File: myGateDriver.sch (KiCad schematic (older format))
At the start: 86 parts, among them Q5 BC817, Q8 TIP41, Q9 TIP42, U2 6N136S, U3 PC817

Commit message: fuse added
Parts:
- removed C?: 100nF, Capacitor_SMD:C_1206_3216Metric_Pad1.33x1.80mm_HandSolder, symbol Device:C
- removed C?: 10uf/35v, Capacitor_THT:CP_Radial_D8.0mm_P3.80mm, symbol Device:CP
- removed CmirrorCurrentProtection: 22nF, Capacitor_SMD:C_1206_3216Metric_Pad1.33x1.80mm_HandSolder, symbol Device:C
- removed D?: 1.5KE10A, Diode_THT:D_DO-201AD_P5.08mm_Vertical_AnodeUp, symbol Diode:1.5KExxA
- removed D?: BYV26E, Diode_THT:D_DO-201AD_P5.08mm_Vertical_AnodeUp, symbol Simulation_SPICE:DIODE
- removed D?: Dz17v, Diode_THT:D_DO-201AD_P5.08mm_Vertical_AnodeUp, symbol Diode:1.5KExxA
- removed Dex3, Dex4: 1n4148, Diode_SMD:D_SMA, symbol Device:D_Schottky
- removed Q? (x3), QDynamicVCE: BC807, Package_TO_SOT_SMD:SOT-23, symbol Transistor_BJT:BC807
- removed Q?: BC817, Package_TO_SOT_SMD:SOT-23, symbol Transistor_BJT:BC817
- removed R10: 220, Resistor_THT:R_Axial_DIN0207_L6.3mm_D2.5mm_P10.16mm_Horizontal, symbol Device:R
- removed Rex?: 1k, Resistor_THT:R_Axial_DIN0207_L6.3mm_D2.5mm_P10.16mm_Horizontal, symbol Device:R
- removed Rex?: 6.8k, Resistor_THT:R_Axial_DIN0207_L6.3mm_D2.5mm_P10.16mm_Horizontal, symbol Device:R
- added D?: 1.5KE6V8A, Diode_THT:D_DO-201AD_P5.08mm_Vertical_AnodeUp, symbol Diode:1.5KExxA
- added F?: Fuse, symbol Device:Fuse
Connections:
- net GND-p: now also Q9.2 (C); no longer Q9.3 (E)
- net Gate: now also JP1.1 (A)
- net Vpp: now also Q5.3 (C), F?.1
- net at CDynamic1.2, DzDynamic1.2 (A2), RDynamic1.2: now also R7.1; no longer JP1.2 (C)
- net Control: now reaches JP1.3 (B)
- net Control: now also CsoftTurnOff2.2, Q8.1 (B), Q9.1 (B), RsoftTurnoff2.2; no longer R7.1
- net at R7.2: now also D?.2 (A2)
- net at Roff1.2: now also Q9.3 (E); no longer Q9.2 (C)
- new net: D?.1 (A1), JP1.2 (C)
- new net Vin: F?.2
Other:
- note added: "Active VCE protection"
- note added: "Control Circuit"
- note added: "Power stage"
- note added: "Under voltage protection"
- note added: "input voltage protection"
- note added: "trun off gate clamp"
- moved on the sheet: C1, C2, C5, C?, CDynamic1, CShortPulseFilter1, CblankTime1, Cclamp1, Cex1, Cex2, CsoftTurnOff2, CsoftTurnOffTiming1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

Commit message: skm200 3d
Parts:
- added SYM1: SYM_Arrow45_Normal, IGBT-DRIVER-emad:skm200GB, symbol Graphic:SYM_Arrow45_Normal
- gave numbers to parts that had none: 11
- renumbered DZunderVoltageFault to DZunderVoltageFault1, DprotectionHigh to DprotectionHigh1, DprotectionLow to DprotectionLow1, QfaultLatch to QfaultLatch1, QsoftTurnOnn to QsoftTurnOnn1
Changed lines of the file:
@@
 P 14450 4875
 AR Path="/630D95A8" Ref="D?"  Part="1"
-AR Path="/6309618D/630D95A8" Ref="DZunderVoltageFault"  Part="1"
+AR Path="/6309618D/630D95A8" Ref="DZunderVoltageFault1"  Part="1"
 AR Path="/63385DDA/630D95A8" Ref="D?"  Part="1"
 AR Path="/6340E1F3/630D95A8" Ref="D22"  Part="1"
-F 0 "DZunderVoltageFault" H 13955 4770 50  0000 L CNN
+F 0 "DZunderVoltageFault1" H 13955 4770 50  0000 L CNN
 F 1 "BZX85C20" H 14250 4985 50  0000 L CNN
 F 2 "Diode_SMD:D_MELF" H 14450 4700 50  0001 C CNN
@@
 P 5865 7905
 AR Path="/630D96CE" Ref="Q?"  Part="1"
-AR Path="/6309618D/630D96CE" Ref="QfaultLatch"  Part="1"
+AR Path="/6309618D/630D96CE" Ref="QfaultLatch1"  Part="1"
 AR Path="/63385DDA/630D96CE" Ref="Q?"  Part="1"
 AR Path="/6340E1F3/630D96CE" Ref="Q17"  Part="1"
-F 0 "QfaultLatch" H 5500 8095 50  0000 L CNN
+F 0 "QfaultLatch1" H 5500 8095 50  0000 L CNN
 F 1 "BC807" H 5610 7760 50  0000 L CNN
 F 2 "Package_TO_SOT_SMD:SOT-23" H 6065 7830 50  0001 L CIN
@@
 P 12755 7520
 AR Path="/61915D54" Ref="Dex?"  Part="1"
-AR Path="/6309618D/61915D54" Ref="DprotectionHigh"  Part="1"
+AR Path="/6309618D/61915D54" Ref="DprotectionHigh1"  Part="1"
 AR Path="/63385DDA/61915D54" Ref="Dex?"  Part="1"
-AR Path="/6340E1F3/61915D54" Ref="Dex?"  Part="1"
-F 0 "DprotectionHigh" H 12675 7625 50  0000 C CNN
+AR Path="/6340E1F3/61915D54" Ref="Dex3"  Part="1"
+F 0 "DprotectionHigh1" H 12675 7625 50  0000 C CNN
 F 1 "1n4148" H 12755 7410 50  0000 C CNN
 F 2 "Diode_SMD:D_SMA" H 12755 7520 50  0001 C CNN
@@
 P 12755 8460
 AR Path="/61941051" Ref="Dex?"  Part="1"
-AR Path="/6309618D/61941051" Ref="DprotectionLow"  Part="1"
+AR Path="/6309618D/61941051" Ref="DprotectionLow1"  Part="1"
 AR Path="/63385DDA/61941051" Ref="Dex?"  Part="1"
-AR Path="/6340E1F3/61941051" Ref="Dex?"  Part="1"
-F 0 "DprotectionLow" H 12745 8565 50  0000 C CNN
+AR Path="/6340E1F3/61941051" Ref="Dex4"  Part="1"
+F 0 "DprotectionLow1" H 12745 8565 50  0000 C CNN
 F 1 "1n4148" H 12755 8350 50  0000 C CNN
 F 2 "Diode_SMD:D_SMA" H 12755 8460 50  0001 C CNN
@@
 P 8005 4040
 AR Path="/61958594" Ref="D?"  Part="1"
-AR Path="/6309618D/61958594" Ref="D?"  Part="1"
+AR Path="/6309618D/61958594" Ref="D7"  Part="1"
 AR Path="/63385DDA/61958594" Ref="D?"  Part="1"
-AR Path="/6340E1F3/61958594" Ref="D?"  Part="1"
-F 0 "D?" V 7920 3995 50  0000 L CNN
+AR Path="/6340E1F3/61958594" Ref="D15"  Part="1"
+F 0 "D7" V 7920 3995 50  0000 L CNN
 F 1 "26v TVS" V 8100 3885 50  0000 L CNN
 F 2 "Diode_SMD:D_MELF" H 8005 3865 50  0001 C CNN
@@
 P 8500 4050
 AR Path="/619A6A28" Ref="C?"  Part="1"
-AR Path="/6309618D/619A6A28" Ref="C?"  Part="1"
+AR Path="/6309618D/619A6A28" Ref="C22"  Part="1"
 AR Path="/63385DDA/619A6A28" Ref="C?"  Part="1"
-AR Path="/6340E1F3/619A6A28" Ref="C?"  Part="1"
-F 0 "C?" H 8505 3985 50  0000 C CNN
+AR Path="/6340E1F3/619A6A28" Ref="C24"  Part="1"
+F 0 "C22" H 8505 3985 50  0000 C CNN
 F 1 "100nF" H 8480 4135 50  0000 C CNN
 F 2 "Capacitor_SMD:C_1206_3216Metric_Pad1.33x1.80mm_HandSolder" H 8538 3900 50  0001 C CNN
@@
 P 7530 4050
 AR Path="/619A742B" Ref="C?"  Part="1"
-AR Path="/6309618D/619A742B" Ref="C?"  Part="1"
+AR Path="/6309618D/619A742B" Ref="C21"  Part="1"
 AR Path="/63385DDA/619A742B" Ref="C?"  Part="1"
-AR Path="/6340E1F3/619A742B" Ref="C?"  Part="1"
-F 0 "C?" H 7525 4125 50  0000 C CNN
+AR Path="/6340E1F3/619A742B" Ref="C23"  Part="1"
+F 0 "C21" H 7525 4125 50  0000 C CNN
 F 1 "47uf/35v" H 7520 3965 50  0000 C CNN
 F 2 "Capacitor_THT:CP_Radial_D8.0mm_P3.80mm" H 7568 3900 50  0001 C CNN
@@
 P 6525 7050
 AR Path="/619F7C8A" Ref="Q?"  Part="1"
-AR Path="/6309618D/619F7C8A" Ref="Q?"  Part="1"
+AR Path="/6309618D/619F7C8A" Ref="Q2"  Part="1"
 AR Path="/63385DDA/619F7C8A" Ref="Q?"  Part="1"
-AR Path="/6340E1F3/619F7C8A" Ref="Q?"  Part="1"
-F 0 "Q?" H 6716 7096 50  0000 L CNN
+AR Path="/6340E1F3/619F7C8A" Ref="Q12"  Part="1"
+F 0 "Q2" H 6716 7096 50  0000 L CNN
 F 1 "BC817" H 6716 7005 50  0000 L CNN
 F 2 "Package_TO_SOT_SMD:SOT-23" H 6725 6975 50  0001 L CIN
@@
 P 6160 8840
 AR Path="/619FC086" Ref="Q?"  Part="1"
-AR Path="/6309618D/619FC086" Ref="QsoftTurnOnn"  Part="1"
+AR Path="/6309618D/619FC086" Ref="QsoftTurnOnn1"  Part="1"
 AR Path="/63385DDA/619FC086" Ref="Q?"  Part="1"
-AR Path="/6340E1F3/619FC086" Ref="Q?"  Part="1"
-F 0 "QsoftTurnOnn" H 6351 8886 50  0000 L CNN
+AR Path="/6340E1F3/619FC086" Ref="Q11"  Part="1"
+F 0 "QsoftTurnOnn1" H 6351 8886 50  0000 L CNN
 F 1 "BC817" H 6351 8795 50  0000 L CNN
 F 2 "Package_TO_SOT_SMD:SOT-23" H 6360 8765 50  0001 L CIN
@@
 P 4655 8770
 AR Path="/619FCED8" Ref="Q?"  Part="1"
-AR Path="/6309618D/619FCED8" Ref="Q?"  Part="1"
+AR Path="/6309618D/619FCED8" Ref="Q1"  Part="1"
 AR Path="/63385DDA/619FCED8" Ref="Q?"  Part="1"
-AR Path="/6340E1F3/619FCED8" Ref="Q?"  Part="1"
-F 0 "Q?" H 4846 8816 50  0000 L CNN
+AR Path="/6340E1F3/619FCED8" Ref="Q10"  Part="1"
+F 0 "Q1" H 4846 8816 50  0000 L CNN
 F 1 "BC817" H 4846 8725 50  0000 L CNN
 F 2 "Package_TO_SOT_SMD:SOT-23" H 4855 8695 50  0001 L CIN
@@
 P 14085 5120
 AR Path="/619FDDB9" Ref="Q?"  Part="1"
-AR Path="/6309618D/619FDDB9" Ref="Q?"  Part="1"
+AR Path="/6309618D/619FDDB9" Ref="Q7"  Part="1"
 AR Path="/63385DDA/619FDDB9" Ref="Q?"  Part="1"
-AR Path="/6340E1F3/619FDDB9" Ref="Q?"  Part="1"
-F 0 "Q?" H 14276 5166 50  0000 L CNN
+AR Path="/6340E1F3/619FDDB9" Ref="Q18"  Part="1"
+F 0 "Q7" H 14276 5166 50  0000 L CNN
 F 1 "BC817" H 14276 5075 50  0000 L CNN
 F 2 "Package_TO_SOT_SMD:SOT-23" H 14285 5045 50  0001 L CIN
@@
 P 11195 4560
 AR Path="/619FFBE7" Ref="Q?"  Part="1"
-AR Path="/6309618D/619FFBE7" Ref="Q?"  Part="1"
+AR Path="/6309618D/619FFBE7" Ref="Q6"  Part="1"
 AR Path="/63385DDA/619FFBE7" Ref="Q?"  Part="1"
-AR Path="/6340E1F3/619FFBE7" Ref="Q?"  Part="1"
-F 0 "Q?" H 11386 4606 50  0000 L CNN
+AR Path="/6340E1F3/619FFBE7" Ref="Q15"  Part="1"
+F 0 "Q6" H 11386 4606 50  0000 L CNN
 F 1 "BC817" H 11386 4515 50  0000 L CNN
 F 2 "Package_TO_SOT_SMD:SOT-23" H 11395 4485 50  0001 L CIN
@@
 P 10780 5000
 AR Path="/61A017AB" Ref="Q?"  Part="1"
-AR Path="/6309618D/61A017AB" Ref="Q?"  Part="1"
+AR Path="/6309618D/61A017AB" Ref="Q3"  Part="1"
 AR Path="/63385DDA/61A017AB" Ref="Q?"  Part="1"
-AR Path="/6340E1F3/61A017AB" Ref="Q?"  Part="1"
-F 0 "Q?" H 10971 5046 50  0000 L CNN
+AR Path="/6340E1F3/61A017AB" Ref="Q13"  Part="1"
+F 0 "Q3" H 10971 5046 50  0000 L CNN
 F 1 "BC817" H 10971 4955 50  0000 L CNN
 F 2 "Package_TO_SOT_SMD:SOT-23" H 10980 4925 50  0001 L CIN
@@
 P 11170 8135
 AR Path="/61926996" Ref="Q?"  Part="1"
-AR Path="/6309618D/61926996" Ref="Q?"  Part="1"
+AR Path="/6309618D/61926996" Ref="Q4"  Part="1"
 AR Path="/63385DDA/61926996" Ref="Q?"  Part="1"
-AR Path="/6340E1F3/61926996" Ref="Q?"  Part="1"
-F 0 "Q?" H 11050 8255 50  0000 L CNN
+AR Path="/6340E1F3/61926996" Ref="Q14"  Part="1"
+F 0 "Q4" H 11050 8255 50  0000 L CNN
 F 1 "BC807" H 11000 7985 50  0000 L CNN
 F 2 "Package_TO_SOT_SMD:SOT-23" H 11370 8060 50  0001 L CIN
@@
 P 4675 1585
 AR Path="/61A66FE0" Ref="D?"  Part="1"
-AR Path="/6309618D/61A66FE0" Ref="D?"  Part="1"
+AR Path="/6309618D/61A66FE0" Ref="D6"  Part="1"
 AR Path="/63385DDA/61A66FE0" Ref="D?"  Part="1"
-AR Path="/6340E1F3/61A66FE0" Ref="D?"  Part="1"
-F 0 "D?" H 4675 1802 50  0000 C CNN
+AR Path="/6340E1F3/61A66FE0" Ref="D12"  Part="1"
+F 0 "D6" H 4675 1802 50  0000 C CNN
 F 1 "1.5KE6V8A" H 4675 1711 50  0000 C CNN
 F 2 "Diode_THT:D_DO-201AD_P5.08mm_Vertical_AnodeUp" H 4675 1385 50  0001 C CNN
@@
 Vin
 $Comp
-L Device:Fuse F?
+L Device:Fuse F2
 U 1 1 61AD0B07
 P 7665 3540
-F 0 "F?" V 7468 3540 50  0000 C CNN
+AR Path="/6309618D/61AD0B07" Ref="F2"  Part="1"
+AR Path="/6340E1F3/61AD0B07" Ref="F4"  Part="1"
+F 0 "F2" V 7468 3540 50  0000 C CNN
 F 1 "Fuse" V 7559 3540 50  0000 C CNN
 F 2 "" V 7595 3540 50  0001 C CNN
@@
 Text Notes 3170 7550 0    50   ~ 0
 Control Circuit
+$Comp
+L Graphic:SYM_Arrow45_Normal SYM1
+U 1 1 61C5788B
+P 780 2520
+AR Path="/6309618D/61C5788B" Ref="SYM1"  Part="1"
+AR Path="/6340E1F3/61C5788B" Ref="#SYM2"  Part="1"
+F 0 "SYM1" H 930 2570 50  0001 C CNN
+F 1 "SYM_Arrow45_Normal" H 780 2420 50  0001 C CNN
+F 2 "IGBT-DRIVER-emad:skm200GB" H 780 2520 50  0001 C CNN
+F 3 "~" H 780 2520 50  0001 C CNN
+	1    780  2520
+	1    0    0    -1
+$EndComp
 $EndSCHEMATC

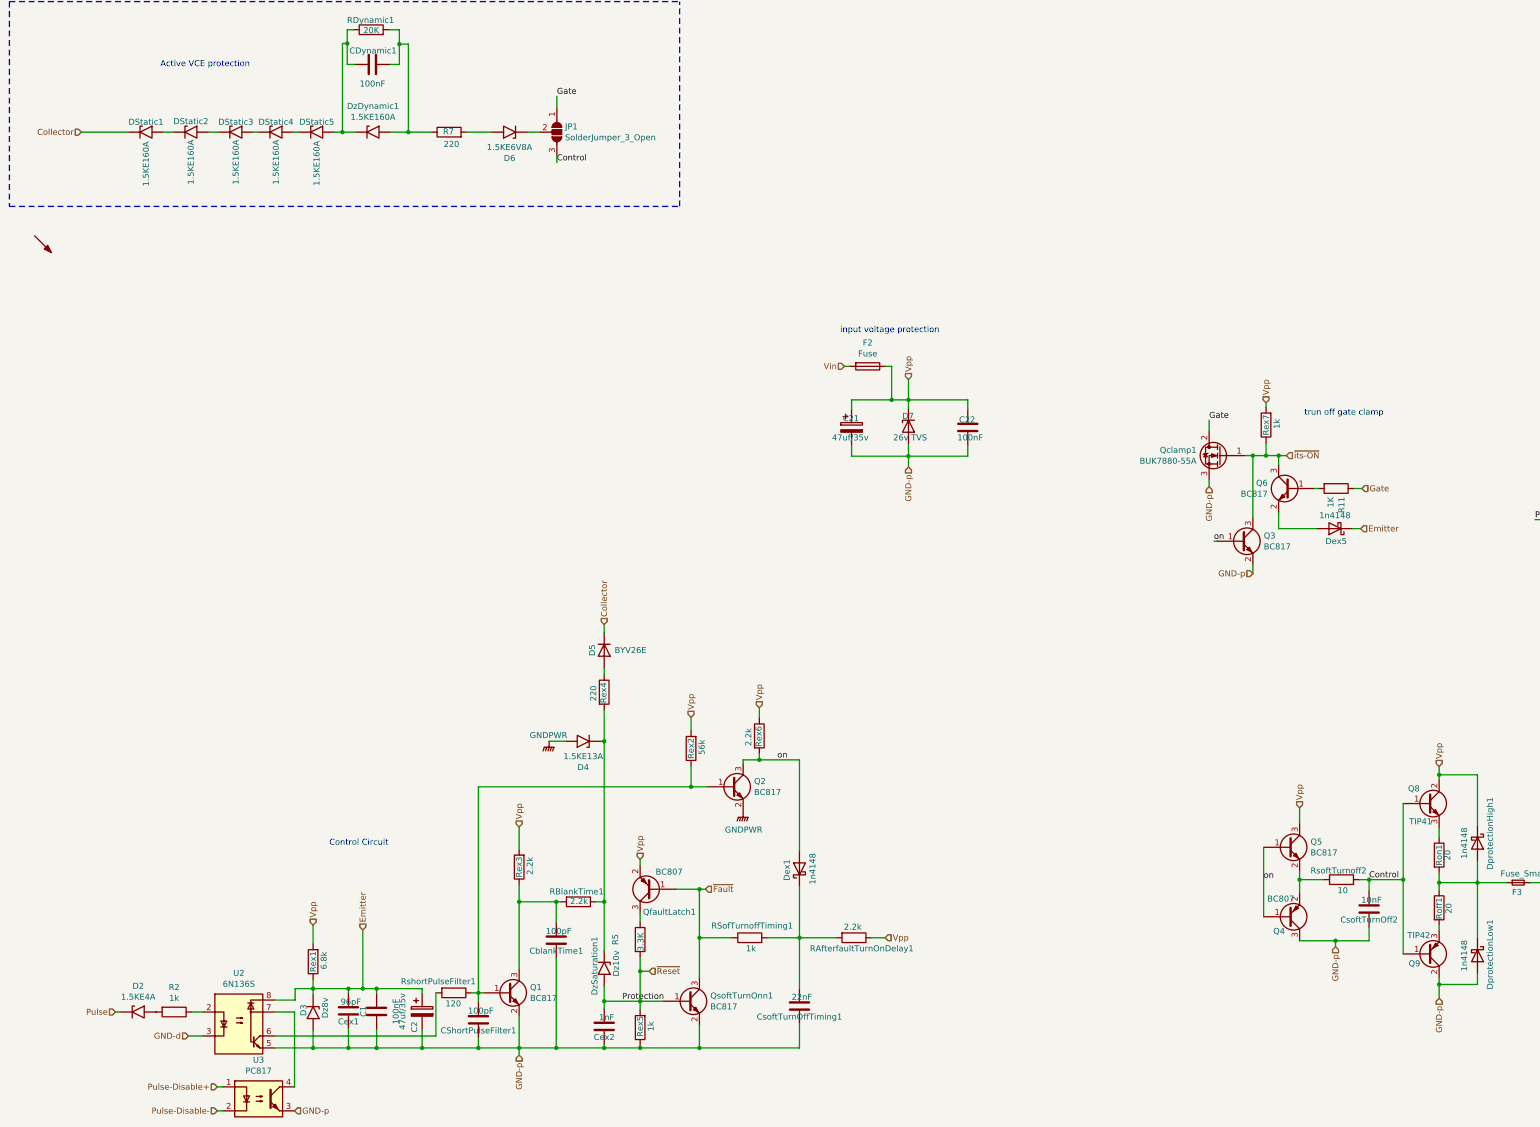
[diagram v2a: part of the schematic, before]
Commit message: changed bjt
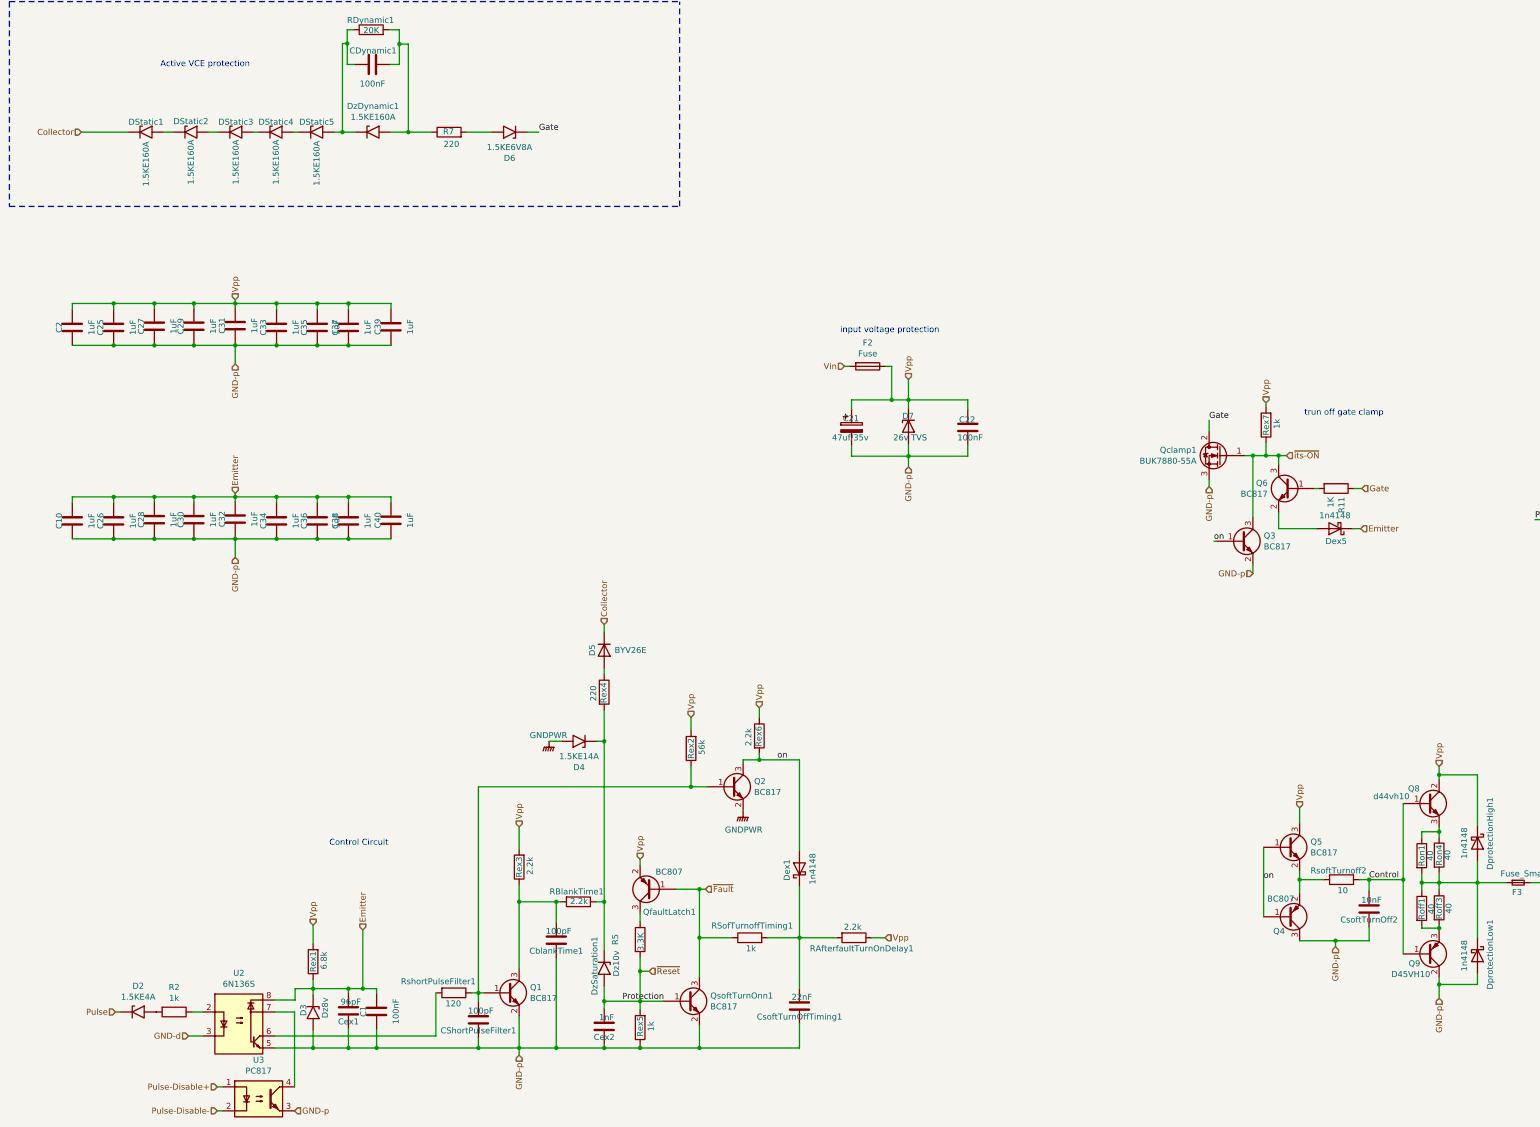
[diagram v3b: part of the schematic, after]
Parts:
- removed C2: 47uf/35v, Capacitor_THT:CP_Radial_D8.0mm_P3.80mm, symbol Device:CP
- removed JP1: SolderJumper_3_Open, symbol Jumper:SolderJumper_3_Open
- removed SYM1: SYM_Arrow45_Normal, IGBT-DRIVER-emad:skm200GB, symbol Graphic:SYM_Arrow45_Normal
- added C10, C2, C25, C26, C27, C28, C29, C30, C31, C32, C33, C34, C35, C36, C37, C38, C39, C40: 1uF, Capacitor_SMD:C_1206_3216Metric_Pad1.33x1.80mm_HandSolder, symbol Device:C
- added Roff1, Ron1: 40, Resistor_SMD:R_2512_6332Metric, symbol Device:R
- CDynamic1: footprint Capacitor_THT:C_Disc_D16.0mm_W5.0mm_P10.00mm -> Capacitor_THT:C_Rect_L16.5mm_W6.0mm_P15.00mm_MKT
- D4: value 1.5KE13A -> 1.5KE14A; footprint Diode_THT:D_DO-201AD_P5.08mm_Vertical_AnodeUp -> Diode_THT:D_DO-201AD_P15.24mm_Horizontal
- D5, D6, DStatic1, DStatic2, DStatic3, DStatic4, DStatic5, DzDynamic1: footprint Diode_THT:D_DO-201AD_P5.08mm_Vertical_AnodeUp -> Diode_THT:D_DO-201AD_P15.24mm_Horizontal
- F2: footprint (none) -> Fuse:Fuse_Schurter_UMZ250
- Q8: value TIP41 -> d44vh10; footprint Package_TO_SOT_THT:TO-220-3_Vertical -> Package_TO_SOT_SMD:TO-252-2
- Q9: value TIP42 -> D45VH10
- R11, R8, R9, RClamp1: footprint Resistor_SMD:R_0805_2012Metric_Pad1.15x1.40mm_HandSolder -> Resistor_SMD:R_0805_2012Metric
- Rex7, RsoftTurnoff2: footprint Resistor_THT:R_Axial_DIN0207_L6.3mm_D2.5mm_P10.16mm_Horizontal -> Resistor_SMD:R_0805_2012Metric
- Roff3: renamed from Roff1; value 20 -> 40; footprint Resistor_THT:R_Axial_DIN0207_L6.3mm_D2.5mm_P10.16mm_Horizontal -> Resistor_SMD:R_2512_6332Metric
- Ron4: renamed from Ron1; value 20 -> 40; footprint Resistor_THT:R_Axial_DIN0207_L6.3mm_D2.5mm_P10.16mm_Horizontal -> Resistor_SMD:R_2512_6332Metric
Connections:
- net Emitter: now also C10.2, C26.2, C28.2, C30.2, C32.2, C34.2, C36.2, C38.2, C40.2
- net GND-p: now also C10.1, C2.1, C25.1, C26.1, C27.1, C28.1, C29.1, C30.1, C31.1, C32.1, C33.1, C34.1, C35.1, C36.1, C37.1, C38.1, C39.1, C40.1
- net Gate: now also D6.1 (A1)
- net Vpp: now also C2.2, C25.2, C27.2, C29.2, C31.2, C33.2, C35.2, C37.2, C39.2
- net at DprotectionHigh1.2 (A), DprotectionLow1.1 (K), F3.1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: now also Roff1.1, Ron1.2
- net at Q8.3 (E), Ron4.1: now also Ron1.1
- net at Q9.3 (E), Roff3.2: now also Roff1.2
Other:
- moved on the sheet: D4

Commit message: some placement
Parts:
- C1, C22, CShortPulseFilter1, CblankTime1, Cex1, Cex2, CsoftTurnOff2, CsoftTurnOffTiming1: footprint Capacitor_SMD:C_1206_3216Metric_Pad1.33x1.80mm_HandSolder -> Capacitor_SMD:C_0805_2012Metric
- Cclamp1: footprint Capacitor_SMD:C_1206_3216Metric -> Capacitor_SMD:C_0805_2012Metric
- F3: footprint gh- kicad:fuse.holder.1808 -> IGBT-DRIVER-emad:fuse.holder.1808
- Q9: footprint Package_TO_SOT_THT:TO-220-3_Vertical -> Package_TO_SOT_SMD:TO-252-2
- R2, R5: footprint Resistor_SMD:R_0805_2012Metric_Pad1.15x1.40mm_HandSolder -> Resistor_SMD:R_0805_2012Metric
- RAfterfaultTurnOnDelay1, RBlankTime1, RSofTurnoffTiming1, Rex1, Rex2, Rex3, Rex4, Rex6, RshortPulseFilter1: footprint Resistor_THT:R_Axial_DIN0207_L6.3mm_D2.5mm_P10.16mm_Horizontal -> Resistor_SMD:R_0805_2012Metric
